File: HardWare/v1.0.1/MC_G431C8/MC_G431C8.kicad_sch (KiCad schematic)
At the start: 9 parts, among them J1 Conn_01x06, J2 Conn_01x03, J3 Conn_01x03, U1 AS5047D

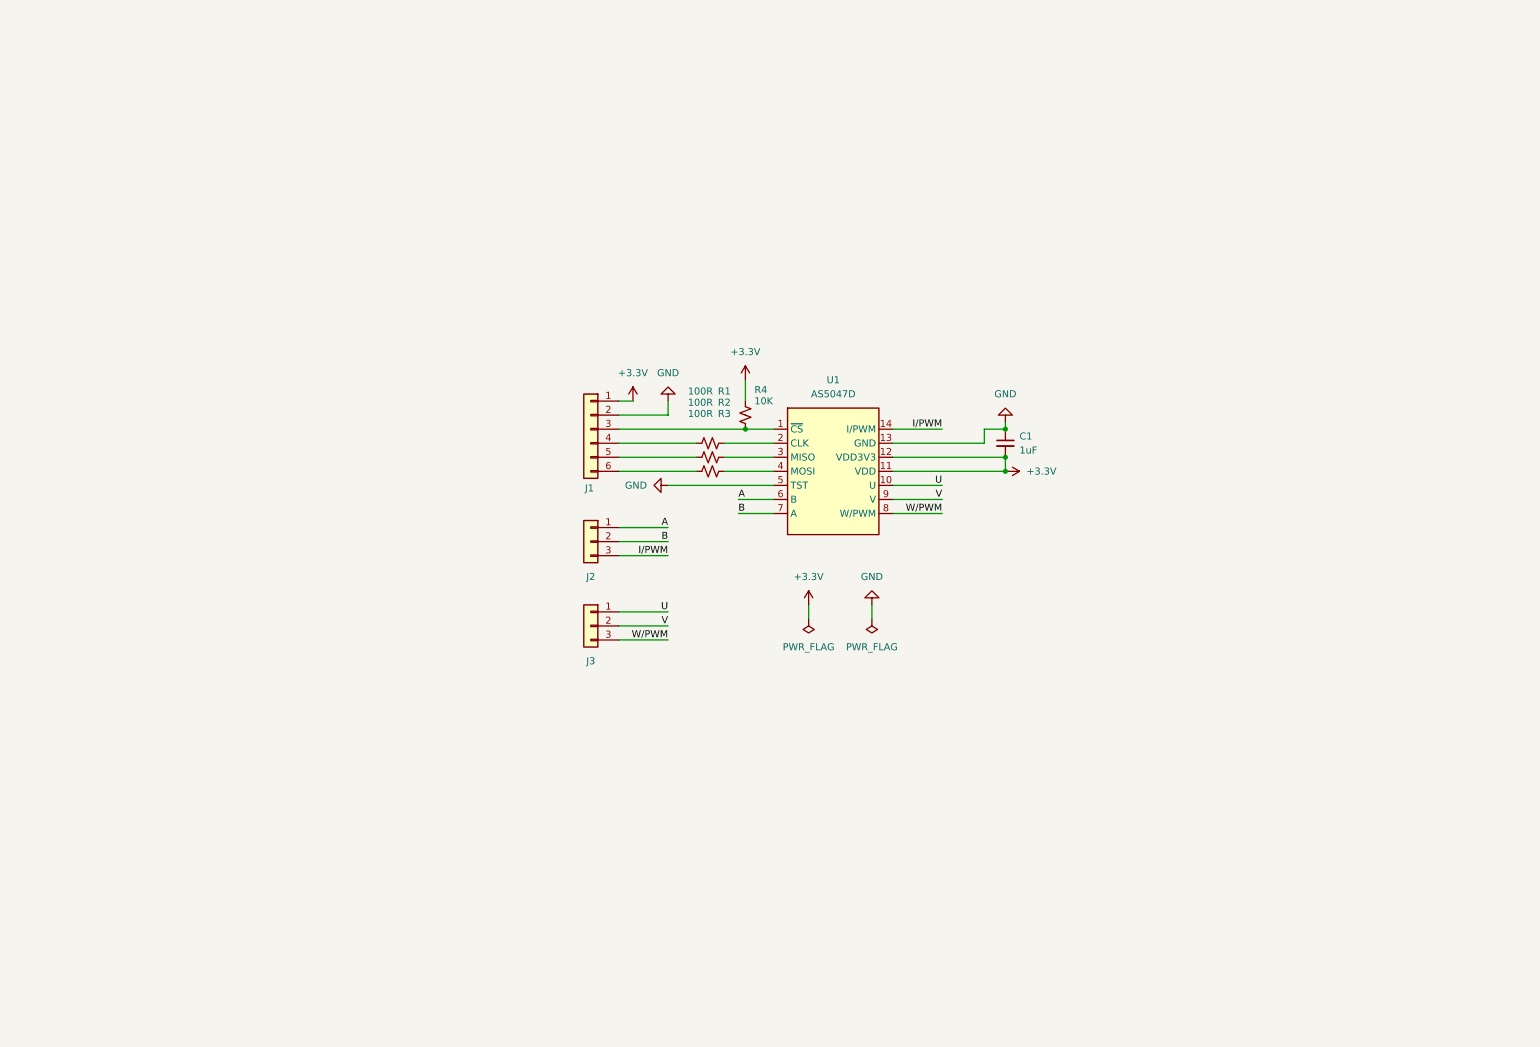
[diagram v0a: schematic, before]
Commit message: 修改硬件版本V02
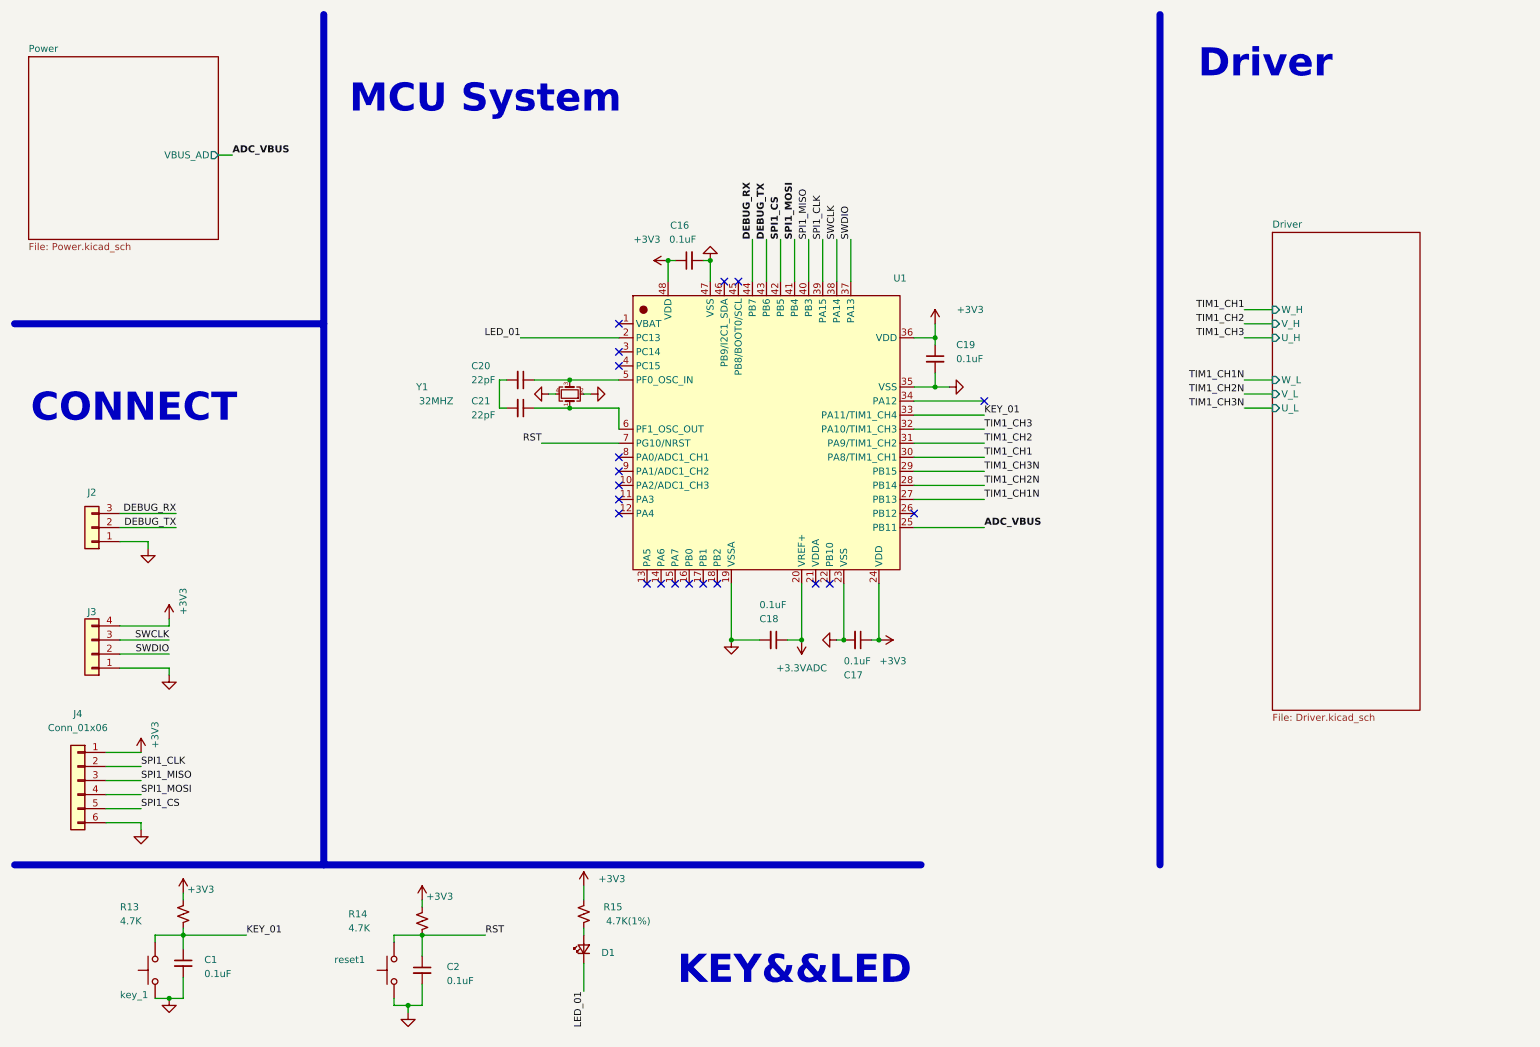
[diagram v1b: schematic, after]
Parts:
- removed J1: Conn_01x06, symbol Connector_Generic:Conn_01x06
- removed J3: Conn_01x03, symbol Connector_Generic:Conn_01x03
- removed R1, R2, R3: 100R, symbol Device:R_Small_US
- removed R4: 10K, symbol Device:R_Small_US
- removed U1: AS5047D, Package_SO:TSSOP-14_4.4x5mm_P0.65mm, symbol User_Sensor:AS5047D
- added C16, C17, C18, C19, C2: 0.1uF, Capacitor_SMD:C_0603_1608Metric, symbol Device:C_Small
- added C20, C21: 22pF, Capacitor_SMD:C_0603_1608Metric, symbol Device:C_Small
- added D1: LED_Red, Diode_SMD:D_0603_1608Metric_Pad1.05x0.95mm_HandSolder, symbol Device:LED_Small
- added J3: Conn_01x04, Connector_PinHeader_2.54mm:PinHeader_1x04_P2.54mm_Vertical, symbol Connector_Generic:Conn_01x04
- added J4: Conn_01x06, Connector_PinHeader_2.54mm:PinHeader_1x06_P2.54mm_Vertical, symbol Connector_Generic:Conn_01x06
- added R13, R14: 4.7K, Resistor_SMD:R_0603_1608Metric, symbol Device:R_Small_US
- added R15: 4.7K(1%), Resistor_SMD:R_0603_1608Metric, symbol Device:R_Small_US
- added U1: ~, Package_QFP:LQFP-48_7x7mm_P0.5mm, symbol User_Mcu:STM32G431C8TX
- added Y1: 32MHZ, Crystal:Crystal_SMD_3225-4Pin_3.2x2.5mm, symbol Device:Crystal_GND24_Small
- added key_1, reset1: SW_Push, Button_Switch_SMD:SW_SPST_CK_RS282G05A3, symbol Switch:SW_Push
- C1: value 1uF -> 0.1uF; footprint (none) -> Capacitor_SMD:C_0603_1608Metric
- J2: footprint (none) -> Connector_PinHeader_2.54mm:PinHeader_1x03_P2.54mm_Vertical
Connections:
- net +3.3V is gone; now on net GND: C1.2
- net A is gone; now on net GND: J2.1 (Pin_1)
- net GND: now also C16.2, C17.2, C18.2, C19.2, C2.2, J3.1 (Pin_1), J4.6 (Pin_6), U1.19 (VSSA), U1.23 (VSS), U1.35 (VSS), U1.47 (VSS), Y1.2, Y1.4, key_1.1, reset1.1; no longer C1.1
- net B renamed DEBUG_TX
- net DEBUG_TX: now also U1.43 (PB6)
- net I/PWM renamed DEBUG_RX
- net DEBUG_RX: now also U1.44 (PB7)
- new net: C20.1, U1.5 (PF0_OSC_IN), Y1.3
- new net: C21.1, U1.6 (PF1_OSC_OUT), Y1.1
- new net: C20.2, C21.2
- new net: D1.2 (A), R15.1
- new net +3.3VADC: C18.1, U1.20 (VREF+)
- new net +3V3: C16.1, C17.1, C19.1, J3.4 (Pin_4), J4.1 (Pin_1), R13.1, R14.1, R15.2, U1.24 (VDD), U1.36 (VDD), U1.48 (VDD)
- new net ADC_VBUS: U1.25 (PB11)
- new net KEY_01: C1.1, R13.2, U1.33 (PA11/TIM1_CH4), key_1.2
- new net LED_01: D1.1 (K), U1.2 (PC13)
- new net RST: C2.1, R14.2, U1.7 (PG10/NRST), reset1.2
- new net SPI1_CLK: J4.2 (Pin_2), U1.39 (PA15)
- new net SPI1_CS: J4.5 (Pin_5), U1.42 (PB5)
- new net SPI1_MISO: J4.3 (Pin_3), U1.40 (PB3)
- new net SPI1_MOSI: J4.4 (Pin_4), U1.41 (PB4)
- new net SWCLK: J3.3 (Pin_3), U1.38 (PA14)
- new net SWDIO: J3.2 (Pin_2), U1.37 (PA13)
- new net TIM1_CH1: U1.30 (PA8/TIM1_CH1)
- new net TIM1_CH1N: U1.27 (PB13)
- new net TIM1_CH2: U1.31 (PA9/TIM1_CH2)
- new net TIM1_CH2N: U1.28 (PB14)
- new net TIM1_CH3: U1.32 (PA10/TIM1_CH3)
- new net TIM1_CH3N: U1.29 (PB15)
- no-connect marks 0 -> 20
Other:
- added sheet Driver (Driver.kicad_sch)
- added sheet Power (Power.kicad_sch)
- note added: "CONNECT"
- note added: "Driver"
- note added: "KEY&&LED"
- note added: "MCU System"

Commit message: 20240603 HardWare优化
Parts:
- U1: value ~ -> STM32G431C8
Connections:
- net +3V3: now also U1.21 (VDDA)
- net OP_I_V: now reaches U1.10 (PA2/ADC1_CH3)
- net OP_I_U: now reaches U1.11 (PA3)
- net OP_I_W: now reaches U1.9 (PA1/ADC1_CH2)
- no-connect marks 20 -> 16
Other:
- sheet Driver ports: added OP_I_U, OP_I_V, OP_I_W; removed none
- note added: "POWER"
- moved on the sheet: J2, J3, J4

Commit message: 20240604 优化硬件原理图及封装
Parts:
- added R49, R50, R51, R52, R53, R54, R55, R56: 100R, Resistor_SMD:R_0603_1608Metric, symbol Device:R_Small_US
- added TP10, TP11, TP12, TP13, TP4, TP5, TP6, TP7, TP8, TP9: TestPoint_Alt, TestPoint:TestPoint_Pad_D1.0mm, symbol Connector:TestPoint_Alt
- J2: footprint Connector_PinHeader_2.54mm:PinHeader_1x03_P2.54mm_Vertical -> Connector_Molex:Molex_PicoBlade_53398-0371_1x03-1MP_P1.25mm_Vertical
- J3: footprint Connector_PinHeader_2.54mm:PinHeader_1x04_P2.54mm_Vertical -> Connector_Molex:Molex_PicoBlade_53398-0471_1x04-1MP_P1.25mm_Vertical
- J4: footprint Connector_PinHeader_2.54mm:PinHeader_1x06_P2.54mm_Vertical -> Connector_Molex:Molex_PicoBlade_53398-0671_1x06-1MP_P1.25mm_Vertical
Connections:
- net ADC_VBUS: now also TP4.1
- net DEBUG_RX: now also R49.1; no longer U1.44 (PB7)
- net DEBUG_TX: now also R50.1; no longer U1.43 (PB6)
- net OP_I_U: now also TP7.1
- net OP_I_V: now also TP6.1
- net OP_I_W: now also TP5.1
- net SPI1_CLK: now also R54.1; no longer U1.39 (PA15)
- net SPI1_CS: now also R51.1; no longer U1.42 (PB5)
- net SPI1_MISO: now also R53.1; no longer U1.40 (PB3)
- net SPI1_MOSI: now also R52.1; no longer U1.41 (PB4)
- net SWCLK: now also R55.1; no longer U1.38 (PA14)
- net SWDIO: now also R56.1; no longer U1.37 (PA13)
- net TIM1_CH1: now also TP8.1
- net TIM1_CH2: now also TP9.1
- net TIM1_CH2N: now also TP12.1
- net TIM1_CH3: now also TP10.1
- net TIM1_CH3N: now also TP13.1
- net ENCODER_A: now reaches U1.14 (PA6)
- net ENCODER_B: now reaches U1.15 (PA7)
- net ENCODER_Z: now reaches U1.16 (PB0)
- new net: R56.2, U1.37 (PA13)
- new net: R55.2, U1.38 (PA14)
- new net: R54.2, U1.39 (PA15)
- new net: R53.2, U1.40 (PB3)
- new net: R52.2, U1.41 (PB4)
- new net: R51.2, U1.42 (PB5)
- new net: R50.2, U1.43 (PB6)
- new net: R49.2, U1.44 (PB7)
- no-connect marks 16 -> 13
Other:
- sheet Driver ports: added AS5047_A, AS5047_B, AS5047_CLK, AS5047_CS, AS5047_MISO, AS5047_MOSI, AS5047_Z; removed none
- moved on the sheet: C16, C17, C18, C19, C20, C21, J2, J3, J4, U1, Y1

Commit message: 20240607 01:44 硬件初步布局已完成
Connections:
- net GND: now also C20.2, C21.2
- net SPI1_CLK: now also R53.1; no longer R54.1
- net SPI1_CS: now also R54.1; no longer R51.1
- net SPI1_MISO: now also R52.1; no longer R53.1
- net SPI1_MOSI: now also R51.1; no longer R52.1
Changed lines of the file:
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@@
 	)
 	(junction
+		(at 95.25 67.31)
+		(diameter 0)
+		(color 0 0 0 0)
+	)
+	(junction
 		(at 40.64 190.5)
 		(diameter 0)
@@
 	(wire
 		(pts
+			(xy 95.25 67.31) (xy 95.25 69.85)
+		)
+		(stroke
+			(width 0)
+			(type default)
+		)
+	)
+	(wire
+		(pts
 			(xy 24.13 114.3) (xy 30.48 114.3)
 		)
@@
 	(wire
 		(pts
-			(xy 95.25 64.77) (xy 95.25 69.85)
+			(xy 95.25 64.77) (xy 95.25 67.31)
 		)
 		(stroke
@@
 	(wire
 		(pts
+			(xy 88.9 67.31) (xy 95.25 67.31)
+		)
+		(stroke
+			(width 0)
+			(type default)
+		)
+	)
+	(wire
+		(pts
 			(xy 163.83 101.6) (xy 163.83 106.68)
 		)
@@
 	)
 	(label "SPI1_MISO"
-		(at 151.13 29.21 90)
+		(at 148.59 29.21 90)
 		(fields_autoplaced yes)
 		(effects
@@
 	)
 	(label "SPI1_MOSI"
-		(at 148.59 29.21 90)
+		(at 146.05 29.21 90)
 		(fields_autoplaced yes)
 		(effects
@@
 	)
 	(label "SPI1_CS"
-		(at 146.05 29.21 90)
+		(at 153.67 29.21 90)
 		(fields_autoplaced yes)
 		(effects
@@
 	)
 	(label "SPI1_CLK"
-		(at 153.67 29.21 90)
+		(at 151.13 29.21 90)
 		(fields_autoplaced yes)
 		(effects
@@
 					(unit 1)
 				)
+			)
+		)
+	)
+	(symbol
+		(lib_name "GND_4")
+		(lib_id "power:GND")
+		(at 88.9 67.31 270)
+		(unit 1)
+		(exclude_from_sim no)
+		(in_bom yes)
+		(on_board yes)
+		(dnp no)
+		(fields_autoplaced yes)
+		(property "Reference" "#PWR064"
+			(at 82.55 67.31 0)
+			(effects
+				(font
+					(size 1.27 1.27)
+				)
+				(hide yes)
+			)
+		)
+		(property "Value" "GND"
+			(at 85.725 67.3101 90)
+			(effects
+				(font
+					(size 1.27 1.27)
+				)
+				(justify right)
+				(hide yes)
+			)
+		)
+		(property "Footprint" ""
+			(at 88.9 67.31 0)
+			(effects
+				(font
+					(size 1.27 1.27)
+				)
+				(hide yes)
+			)
+		)
+		(property "Datasheet" ""
+			(at 88.9 67.31 0)
+			(effects
+				(font
+					(size 1.27 1.27)
+				)
+				(hide yes)
+			)
+		)
+		(property "Description" "Power symbol creates a global label with name \"GND\" , ground"
+			(at 88.9 67.31 0)
+			(effects
+				(font
+					(size 1.27 1.27)
+				)
+				(hide yes)
+			)
+		)
+		(pin "1"
+		)
+		(instances
+			(project "MC_G431C8"
+				(path "/b9096835-a1ea-44bb-ab3c-f1fee24a7f90"
+					(reference "#PWR064")
+					(unit 1)
+				)

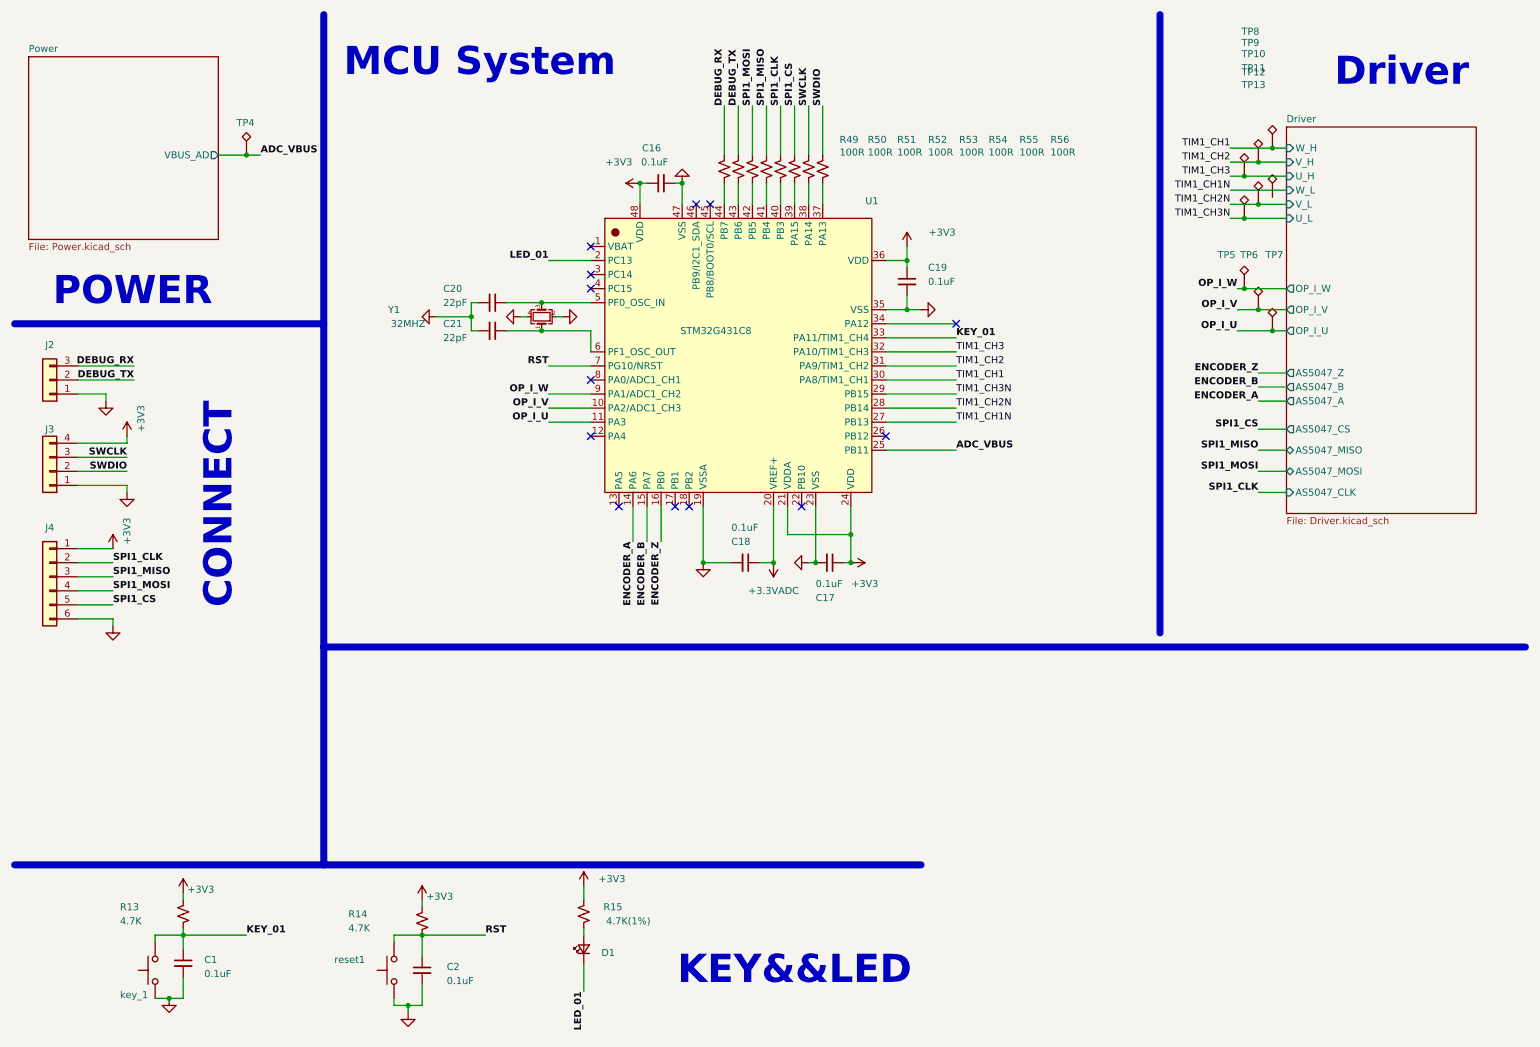
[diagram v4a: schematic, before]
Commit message: 20240608 增加Can电路，优化整体布局
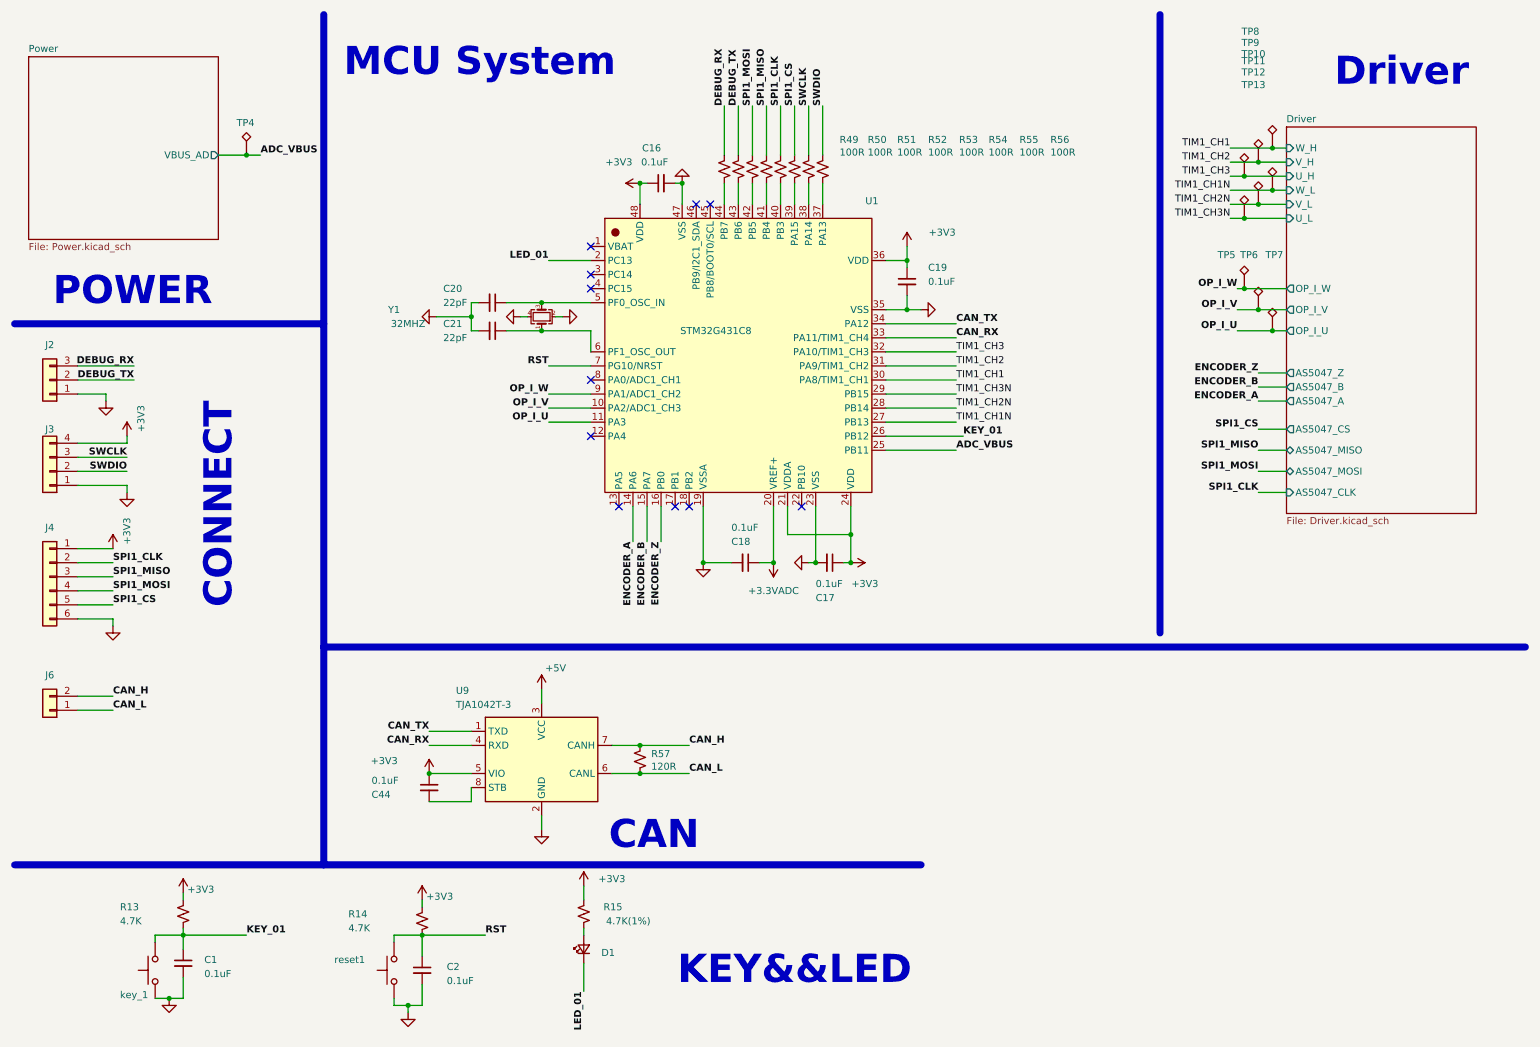
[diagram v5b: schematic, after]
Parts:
- added C44: 0.1uF, Capacitor_SMD:C_0603_1608Metric, symbol Device:C_Small
- added J6: Conn_01x02, Connector_Molex:Molex_PicoBlade_53398-0271_1x02-1MP_P1.25mm_Vertical, symbol Connector_Generic:Conn_01x02
- added R57: 120R, Resistor_SMD:R_0603_1608Metric, symbol Device:R_Small_US
- added U9: TJA1042T-3, Package_SO:SOIC-8_3.9x4.9mm_P1.27mm, symbol Interface_CAN_LIN:TJA1042T-3
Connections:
- net +3V3: now also C44.1, U9.5 (VIO)
- net GND: now also U9.2 (GND)
- net KEY_01: now also U1.26 (PB12); no longer U1.33 (PA11/TIM1_CH4)
- net TIM1_CH1N: now also TP11.1
- net CAN_TX: now reaches U1.34 (PA12)
- net CAN_TX: now also U9.1 (TXD)
- new net: C44.2, U9.8 (STB)
- new net +5V: U9.3 (VCC)
- new net CAN_H: J6.2 (Pin_2), R57.1, U9.7 (CANH)
- new net CAN_L: J6.1 (Pin_1), R57.2, U9.6 (CANL)
- new net CAN_RX: U1.33 (PA11/TIM1_CH4), U9.4 (RXD)
- no-connect marks 13 -> 11
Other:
- note added: "CAN"
- moved on the sheet: TP11
